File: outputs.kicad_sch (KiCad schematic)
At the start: 24 parts, among them J10 B2B-PH-K-S, J11 B16B-PH-SM4-TB_LF__SN_, J12 532610971, J7 B2B-PH-K-S, J8 B2B-PH-K-S, J9 Conn_01x24_FFC_0.5mm_AFC01-S2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, Q6 AO3400A, Q7 AO3400A, U19 DFR0299

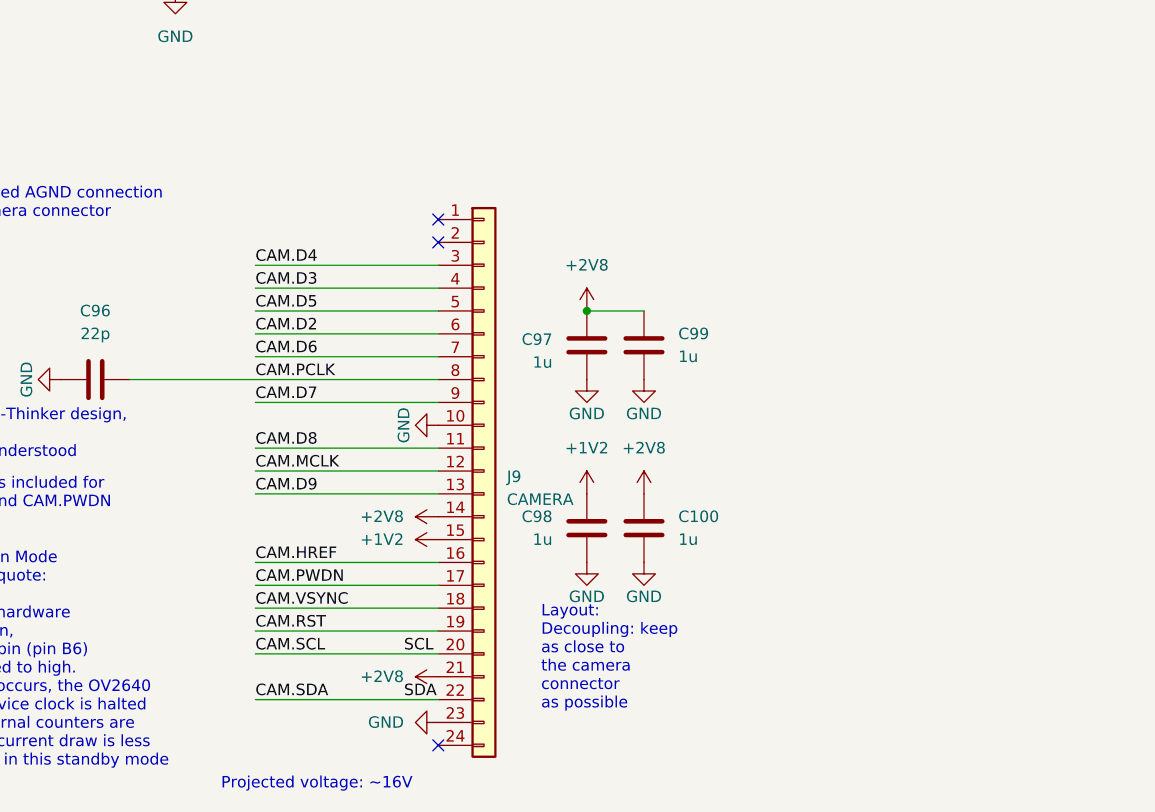
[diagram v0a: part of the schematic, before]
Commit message: GPIOs shouldn't have any conflicts
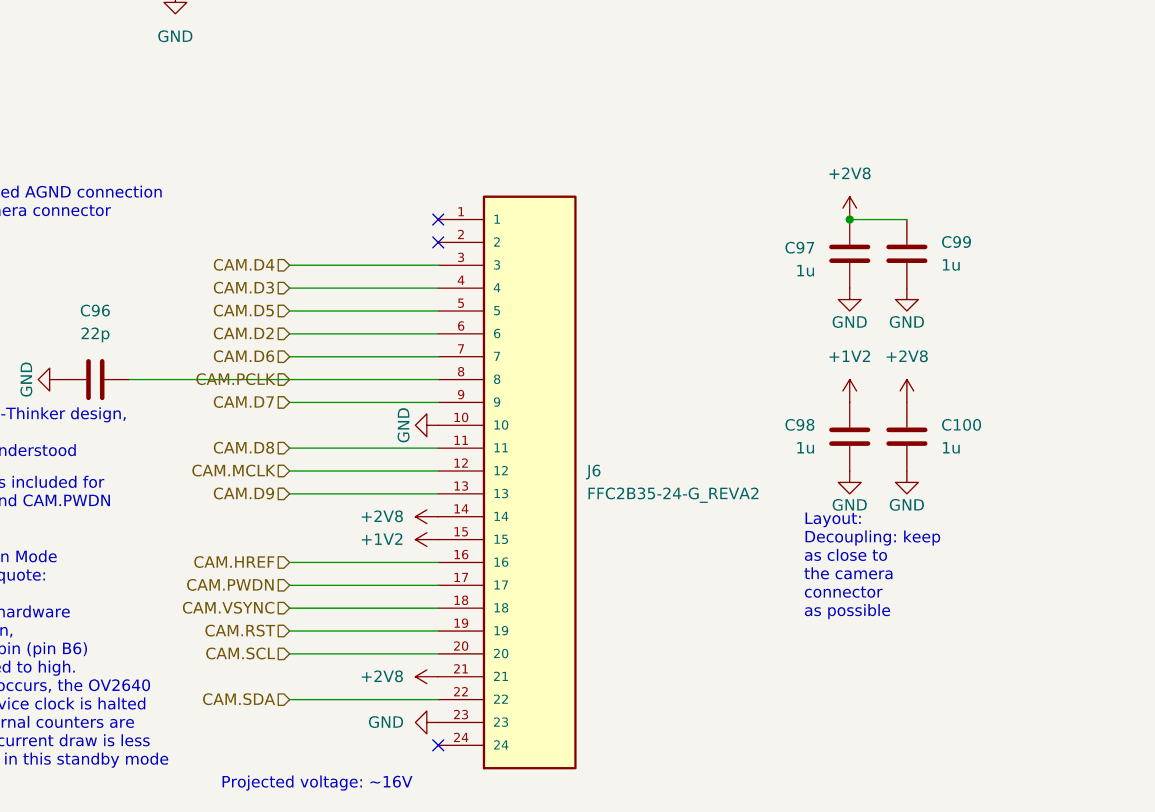
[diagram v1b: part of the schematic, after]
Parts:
- removed J9: Conn_01x24_FFC_0.5mm_AFC01-S24FCC-00, 00-kiml-connector-fpc-ffc:Jushuo_AFC01-S24FCC-00_1x24-1MP_P0.50_Horizontal, symbol 00-kiml-connector-fpc-ffc:Conn_01x24_FFC_0.5mm_AFC01-S24FCC-00
- added J6: FFC2B35-24-G_REVA2, FFC2B35-24-G_REVA2:GCT_FFC2B35-24-G_REVA2, symbol FFC2B35-24-G_REVA2:FFC2B35-24-G_REVA2
- J11: footprint B16BPHSM4TBLFSN -> B16B-PH-SM4-TB_LF__SN_:B16BPHSM4TBLFSN
- J12: footprint CONN_532610001-SD_09_MOL -> 532610971:CONN_532610001-SD_09_MOL
- R89, R90, R91, R92: footprint (none) -> Resistor_SMD:R_0603_1608Metric
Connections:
- net +1V2: now also J6.15
- net +2V8: now also J6.14, J6.21
- net CAM.D2: now also J6.6
- net CAM.D3: now also J6.4
- net CAM.D4: now also J6.3
- net CAM.D5: now also J6.5
- net CAM.D6: now also J6.7
- net CAM.D7: now also J6.9
- net CAM.D8: now also J6.11
- net CAM.D9: now also J6.13
- net CAM.HREF: now also J6.16
- net CAM.MCLK: now also J6.12
- net CAM.PCLK: now also J6.8
- net CAM.PWDN: now also J6.17
- net CAM.RST: now also J6.19
- net CAM.SCL: now also J6.20
- net CAM.SDA: now also J6.22
- net CAM.VSYNC: now also J6.18
- net GND: now also J6.10, J6.23
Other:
- moved on the sheet: C100, C97, C98, C99

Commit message: put all the components on the pcb on traces
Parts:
- removed C100, C101, C97, C98, C99: 10u_0402_CL05A105KA5NQNC, Capacitor_SMD:C_0402_1005Metric, symbol 00-kiml-capacitors-smd:1u_0402_CL05A105KA5NQNC
- removed C96: 22p_0402_0402CG220J500NT, Capacitor_SMD:C_0402_1005Metric, symbol 00-kiml-capacitors-smd:22p_0402_0402CG220J500NT
- removed H5, H6, H7, H8: MountingHole_Pad, MountingHole:MountingHole_3.2mm_M3_Pad_TopBottom, symbol Mechanical:MountingHole_Pad
- removed J6: FFC2B35-24-G_REVA2, FFC2B35-24-G_REVA2:GCT_FFC2B35-24-G_REVA2, symbol FFC2B35-24-G_REVA2:FFC2B35-24-G_REVA2
- removed R93: 215k_0402_0402WGD2153TCE, Resistor_SMD:R_0402_1005Metric, symbol 00-kiml-resistors-smd:215k_0402_0402WGD2153TCE
- added C39, C44: 470uF, Capacitor_THT:CP_Radial_D10.0mm_P5.00mm, symbol Device:C
- added J6: B6B-PH-SM4-TB, B6B-PH-SM4-TB:JST_B6B-PH-SM4-TB, symbol B6B-PH-SM4-TB:B6B-PH-SM4-TB
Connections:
- net +12V: now also C39.2, C44.2
- net +3V3: now also U19.1 (VCC), J6.1
- net +5V: no longer U19.1 (VCC)
- net GND: now also C39.1, C44.1, J6.2
- new net CAM_SD_MISO: J6.4
- new net CAM_SD_MOSI: J6.5
- new net CAM_SD_SCLK: J6.3
- new net ~{CAM_CS}: J6.6
- no-connect marks 5 -> 2
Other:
- note removed: "Bus connections to ESP32 MCU are optimized for easier layout"
- note removed: "Found in AI-Thinker design, purpose is yet to be understood"
- note removed: "Layout: Decoupling: keep as close to the camera connector as possible"
- note removed: "Layout: form a loop of GNDPWR around the PCB Do a via stitching with a spacing <= 20mm (resonant freq of the via cell is ~15 GHz)"
- note removed: "Power Down Mode datasheet quote: To initiate hardware power-down, the PWDN pin (pin B6) must be tied to high. When this occurs, the OV2640 internal device clock is halted and all internal counters are reset. The current draw is less than 15 µA in this standby mode"
- note removed: "Projected voltage: ~16V"
- note removed: "Pull-down is included for CAM.RST and CAM.PWDN internally."
- note removed: "TODO: decide if sophisticated AGND connection (layout) is required for camera connector"

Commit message: wip - started traces for layout
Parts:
- added J10: 878980204, 87898-0204:87898-0204_MOL, symbol 87898-0204:878980204
- renumbered C39 to C62, C44 to C63, J7 to J6, J6 to J7, J10 to J9, R89 to R65, R90 to R66, R91 to R67, R92 to R68, U19 to U13
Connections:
- net BUZZ renamed BUZZ/USB-
- net BUZZ/USB-: now also J10.2
- net STROBE renamed STROBE/USB+
- net STROBE/USB+: now also J10.1
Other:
- note added: "Remove R90 and R92 to use debugger USB+/-"
